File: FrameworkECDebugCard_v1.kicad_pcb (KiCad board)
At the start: 2 copper layers, 23.8 x 28 mm, 29 parts, among them J1 Conn_01x05, P1 1054440011, P2 2169900001, U1 FT230XS

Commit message: ec3: fix typo
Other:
- board text added: "Designed by @DHowett in 2025 under the patronage of His Excellency King Rigsby. Long may he reign."
- board text removed: "Designed by @DHowett in 2025 under the patronage of His Excellency king Rigsby. Long may he reign."
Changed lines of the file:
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@@
 		)
 	)
-	(gr_text "Designed by @DHowett\nin 2025 under the\npatronage of His\nExcellency king\nRigsby. Long may\nhe reign."
+	(gr_text "Designed by @DHowett\nin 2025 under the\npatronage of His\nExcellency King\nRigsby. Long may\nhe reign."
 		(at 150.53 139.92 0)
 		(layer "B.SilkS")

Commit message: Add JLCPCB LCSC part numbers
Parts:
- D2: value KT-0603G -> KT-0603W
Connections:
- P2 pad SH1: GND -> (no net)
- P2 pad SH2: GND -> (no net)
- P2 pad SH3: GND -> (no net)
- P2 pad SH4: GND -> (no net)

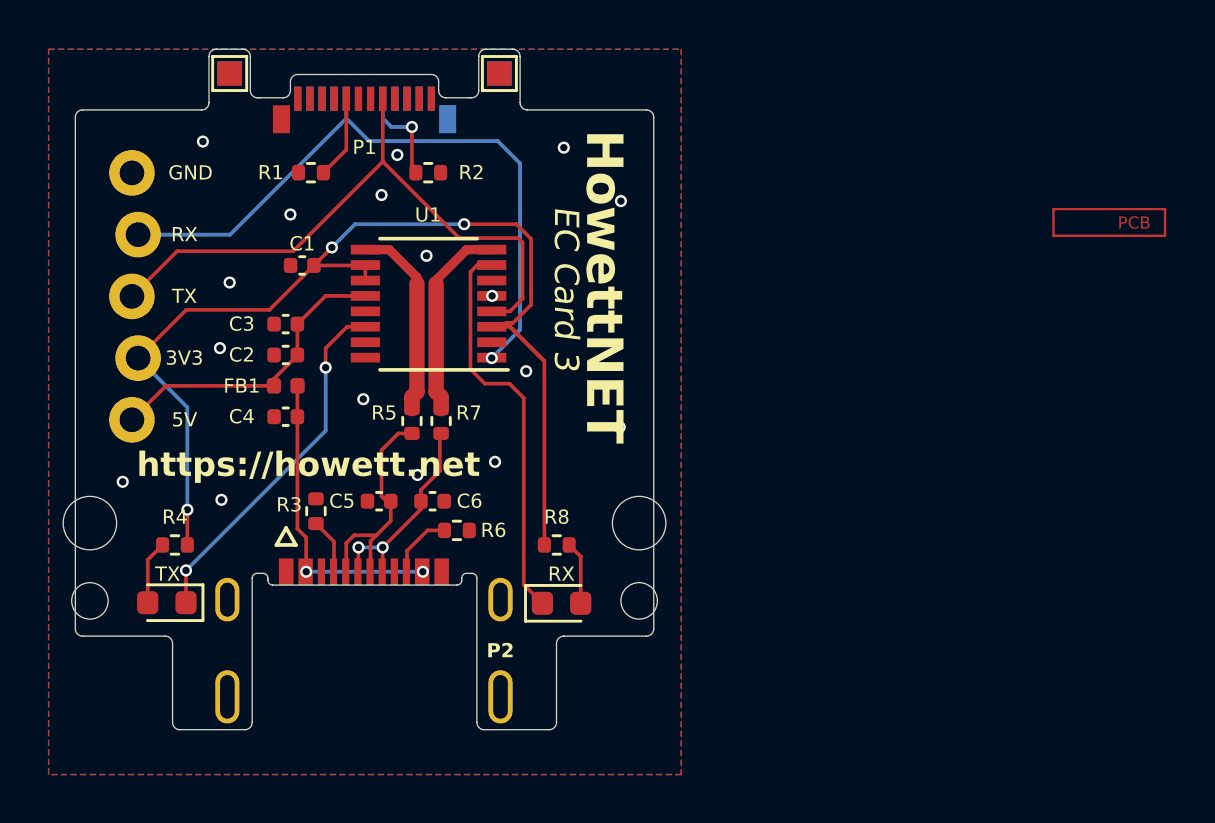
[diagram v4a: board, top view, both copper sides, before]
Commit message: Remove vias-in-pad
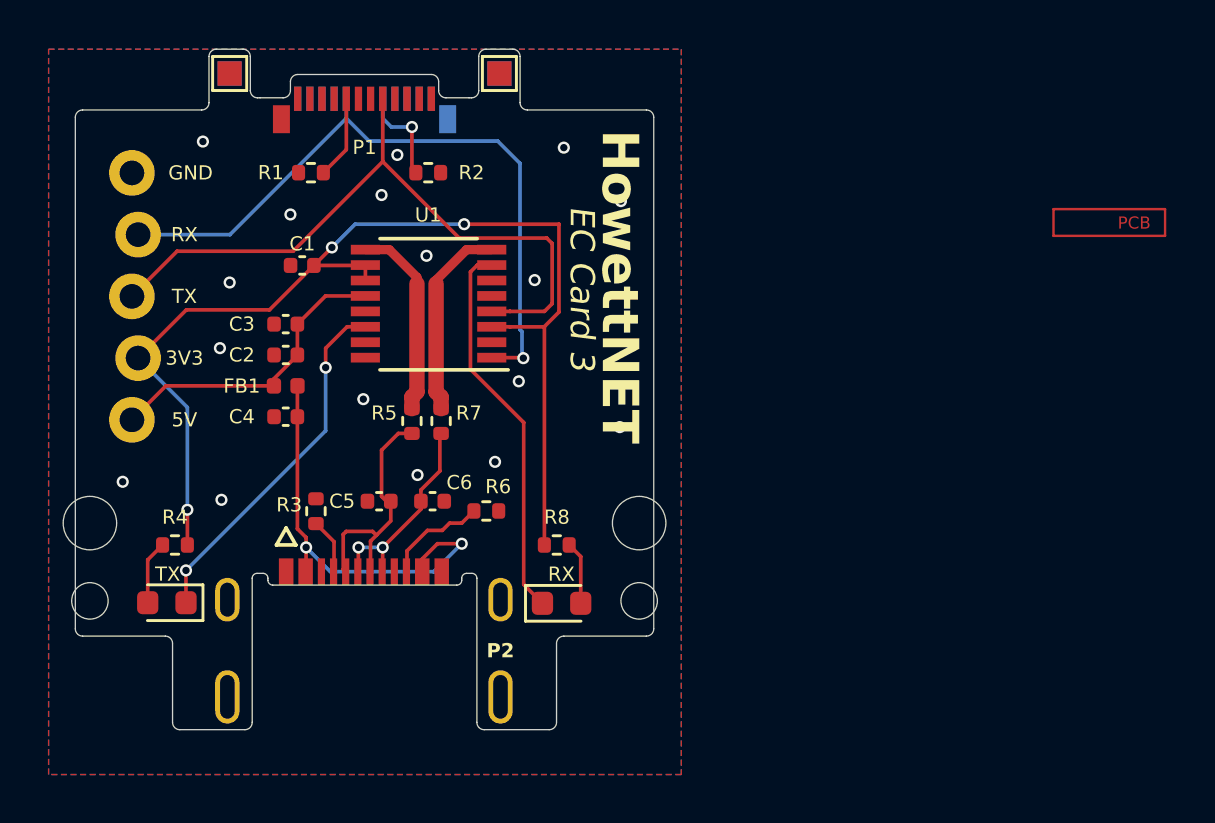
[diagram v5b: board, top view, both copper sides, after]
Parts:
- moved R6 1.45 mm to (145.0, 146.0)
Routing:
- net Net-(C4-Pad1): track 12.6 -> 17.5 mm
- net /DOUT: track 26.1 -> 28.7 mm
- net Net-(P2-CC2): track 2.75 -> 4.29 mm
- net /DIN: track 27.8 -> 28.6 mm
- net /RXLED: track 16.4 -> 15.9 mm
- net /USBD-: track 9.69 -> 10.2 mm
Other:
- board text removed: "https://howett.net"
